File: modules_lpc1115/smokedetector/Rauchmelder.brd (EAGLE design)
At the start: 38 x 65 mm, 75 parts, among them IC100 BD9G101, IC2 LPC1115, Q1 BC856, Q3 BCP52, Q4 ASFL, T1 BC847C, T2 BC817

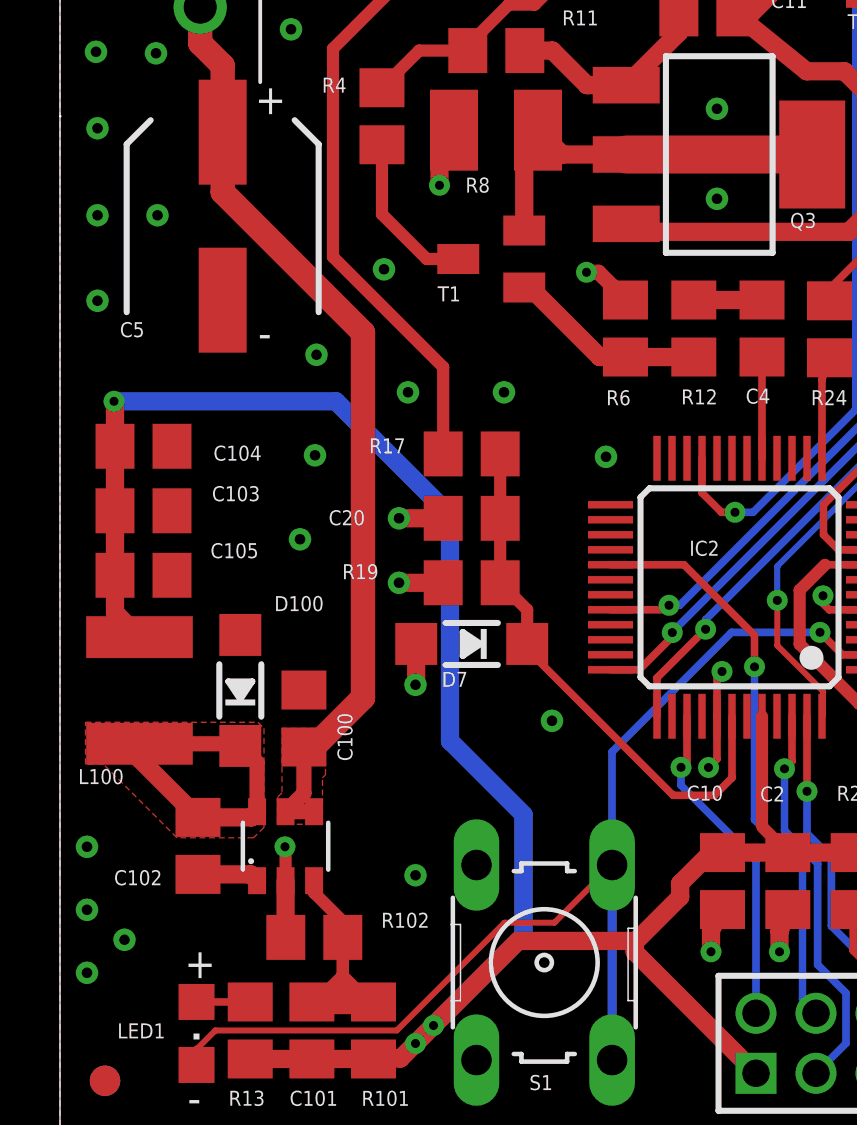
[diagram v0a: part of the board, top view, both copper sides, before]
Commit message: [RM] - bigger footprints for D100 and C100 for easier part sourcing
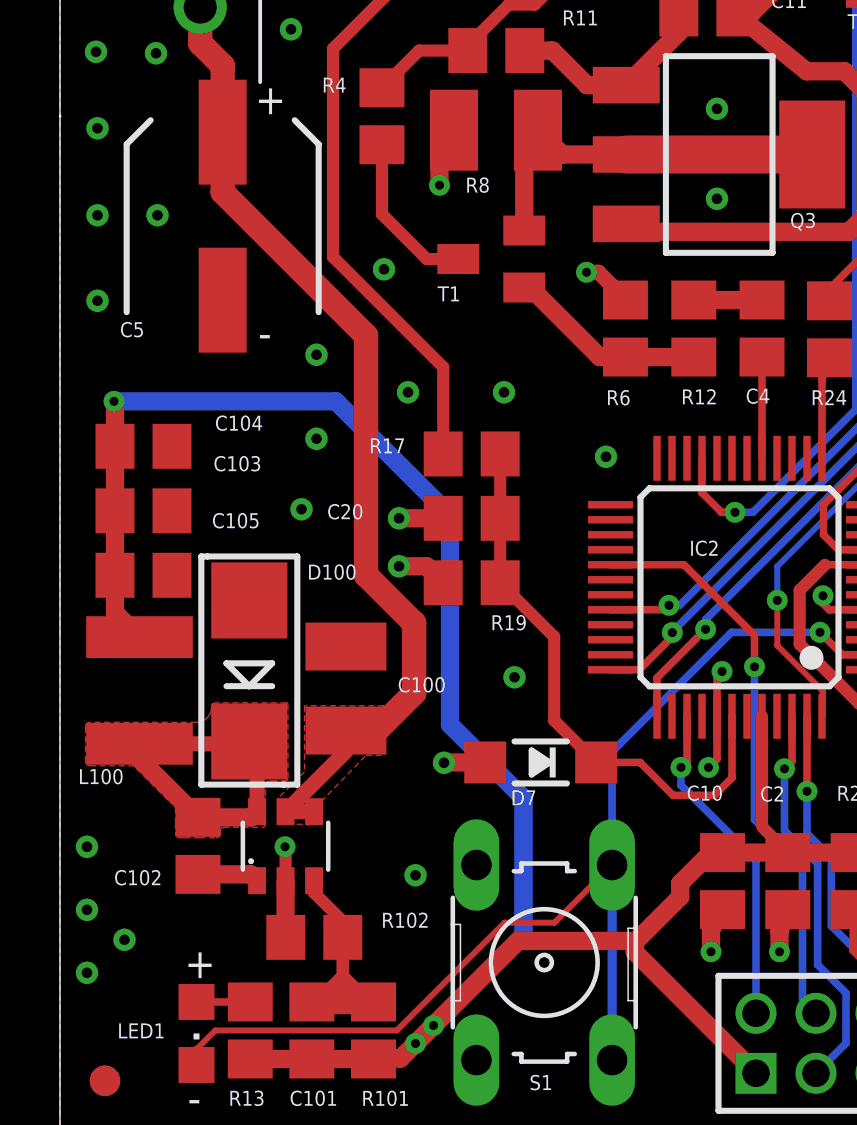
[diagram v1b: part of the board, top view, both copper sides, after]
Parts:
- C100: device rcl:C0805 -> rcl:C1210
- D100: device microbuilder:SOD-123 -> SamacSys_Parts:SMADIODE
- moved D7 4.57 mm to (16.0, 12.1)
- moved C100 1.72 mm to (9.53, 14.6)
- moved D100 0.72 mm to (6.31, 15.2)
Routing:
- net EIB_DC: track 49.1 -> 50.3 mm
- net BUS_V1: track 18.0 -> 18.9 mm
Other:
- board text added: "Selfbus RM-ARM v3.9.1"
- board text removed: "Selfbus RM-ARM v3.9.0"
